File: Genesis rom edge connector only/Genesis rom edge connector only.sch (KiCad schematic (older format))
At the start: 3 parts, among them J1 Conn_02x32_Top_Bottom, J2 Conn_01x32_Male, J3 Conn_01x32_Male

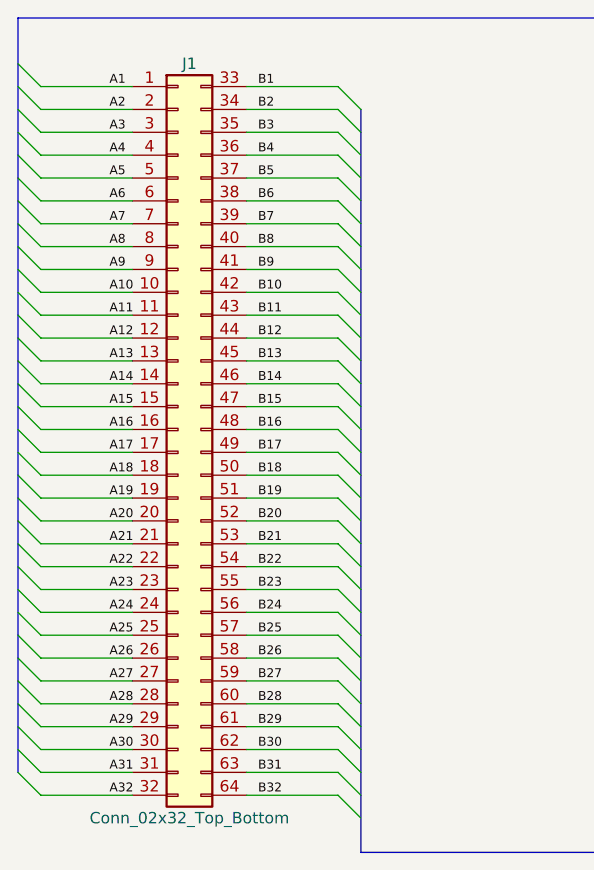
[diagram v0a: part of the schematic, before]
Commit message: basic flash functions are working
Finished implementing basic flash functions: read byte, write byte, erase  all, check mem type.
Fixed silk screen typo on pcb.
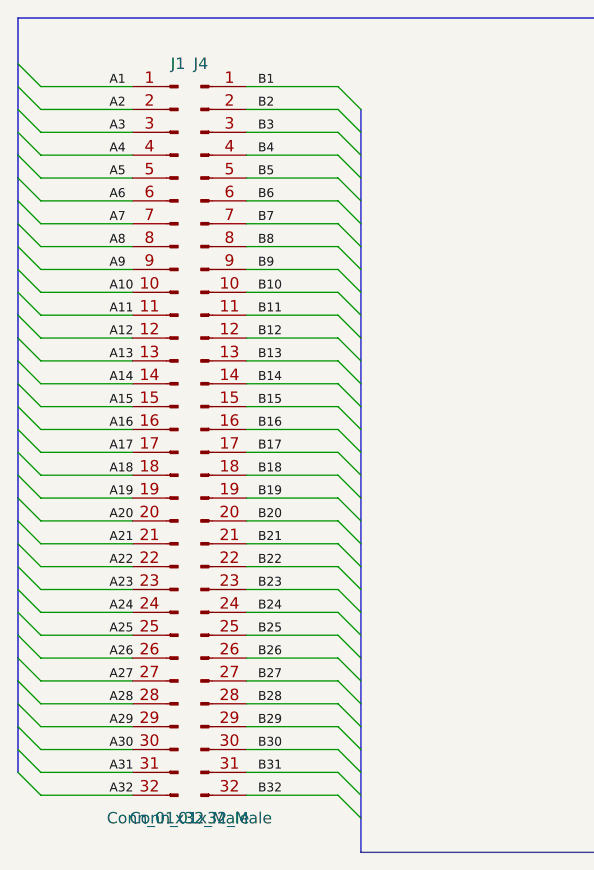
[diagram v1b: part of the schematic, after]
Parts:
- removed J1: Conn_02x32_Top_Bottom, Connectors_Edge:Sega Genesis, symbol Conn_02x32_Top_Bottom
- added J1, J4: Conn_01x32_Male, Connectors_Edge:Sega_Genesis, symbol Conn_01x32_Male
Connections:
- net A1: now also J1.1 (Pin_1)
- net A10: now also J1.10 (Pin_10)
- net A11: now also J1.11 (Pin_11)
- net A12: now also J1.12 (Pin_12)
- net A13: now also J1.13 (Pin_13)
- net A14: now also J1.14 (Pin_14)
- net A15: now also J1.15 (Pin_15)
- net A16: now also J1.16 (Pin_16)
- net A17: now also J1.17 (Pin_17)
- net A18: now also J1.18 (Pin_18)
- net A19: now also J1.19 (Pin_19)
- net A2: now also J1.2 (Pin_2)
- net A20: now also J1.20 (Pin_20)
- net A21: now also J1.21 (Pin_21)
- net A22: now also J1.22 (Pin_22)
- net A23: now also J1.23 (Pin_23)
- net A24: now also J1.24 (Pin_24)
- net A25: now also J1.25 (Pin_25)
- net A26: now also J1.26 (Pin_26)
- net A27: now also J1.27 (Pin_27)
- net A28: now also J1.28 (Pin_28)
- net A29: now also J1.29 (Pin_29)
- net A3: now also J1.3 (Pin_3)
- net A30: now also J1.30 (Pin_30)
- net A31: now also J1.31 (Pin_31)
- net A32: now also J1.32 (Pin_32)
- net A4: now also J1.4 (Pin_4)
- net A5: now also J1.5 (Pin_5)
- net A6: now also J1.6 (Pin_6)
- net A7: now also J1.7 (Pin_7)
- net A8: now also J1.8 (Pin_8)
- net A9: now also J1.9 (Pin_9)
- net B1: now also J4.1 (Pin_1)
- net B10: now also J4.10 (Pin_10)
- net B11: now also J4.11 (Pin_11)
- net B12: now also J4.12 (Pin_12)
- net B13: now also J4.13 (Pin_13)
- net B14: now also J4.14 (Pin_14)
- net B15: now also J4.15 (Pin_15)
- net B16: now also J4.16 (Pin_16)
- net B17: now also J4.17 (Pin_17)
- net B18: now also J4.18 (Pin_18)
- net B19: now also J4.19 (Pin_19)
- net B2: now also J4.2 (Pin_2)
- net B20: now also J4.20 (Pin_20)
- net B21: now also J4.21 (Pin_21)
- net B22: now also J4.22 (Pin_22)
- net B23: now also J4.23 (Pin_23)
- net B24: now also J4.24 (Pin_24)
- net B25: now also J4.25 (Pin_25)
- net B26: now also J4.26 (Pin_26)
- net B27: now also J4.27 (Pin_27)
- net B28: now also J4.28 (Pin_28)
- net B29: now also J4.29 (Pin_29)
- net B3: now also J4.3 (Pin_3)
- net B30: now also J4.30 (Pin_30)
- net B31: now also J4.31 (Pin_31)
- net B32: now also J4.32 (Pin_32)
- net B4: now also J4.4 (Pin_4)
- net B5: now also J4.5 (Pin_5)
- net B6: now also J4.6 (Pin_6)
- net B7: now also J4.7 (Pin_7)
- net B8: now also J4.8 (Pin_8)
- net B9: now also J4.9 (Pin_9)
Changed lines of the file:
@@
 $EndDescr
-$Comp
-L Conn_02x32_Top_Bottom J1
-U 1 1 5BB104DD
-P 2300 2900
-F 0 "J1" H 2350 4500 50  0000 C CNN
-F 1 "Conn_02x32_Top_Bottom" H 2350 1200 50  0000 C CNN
-F 2 "Connectors_Edge:Sega Genesis" H 2300 2900 50  0001 C CNN
-F 3 "" H 2300 2900 50  0001 C CNN
-	1    2300 2900
-	1    0    0    -1
-$EndComp
 $Comp
 L Conn_01x32_Male J2
@@
 Text Label 7100 1400 0    39   ~ 0
 B1
+$Comp
+L Conn_01x32_Male J1
+U 1 1 5BB16D1F
+P 2300 2900
+F 0 "J1" H 2300 4500 50  0000 C CNN
+F 1 "Conn_01x32_Male" H 2300 1200 50  0000 C CNN
+F 2 "Connectors_Edge:Sega_Genesis" H 2300 2900 50  0001 C CNN
+F 3 "" H 2300 2900 50  0001 C CNN
+	1    2300 2900
+	-1   0    0    -1
+$EndComp
+$Comp
+L Conn_01x32_Male J4
+U 1 1 5BB16D77
+P 2400 2900
+F 0 "J4" H 2400 4500 50  0000 C CNN
+F 1 "Conn_01x32_Male" H 2400 1200 50  0000 C CNN
+F 2 "Connectors_Edge:Sega_Genesis" H 2400 2900 50  0001 C CNN
+F 3 "" H 2400 2900 50  0001 C CNN
+	1    2400 2900
+	1    0    0    -1
+$EndComp
 $EndSCHEMATC
